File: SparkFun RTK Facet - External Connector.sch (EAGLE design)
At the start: 29 parts, among them J1 Qwiic, J3 ESP32 USB, J4 Qwiic, J5 u-blox USB

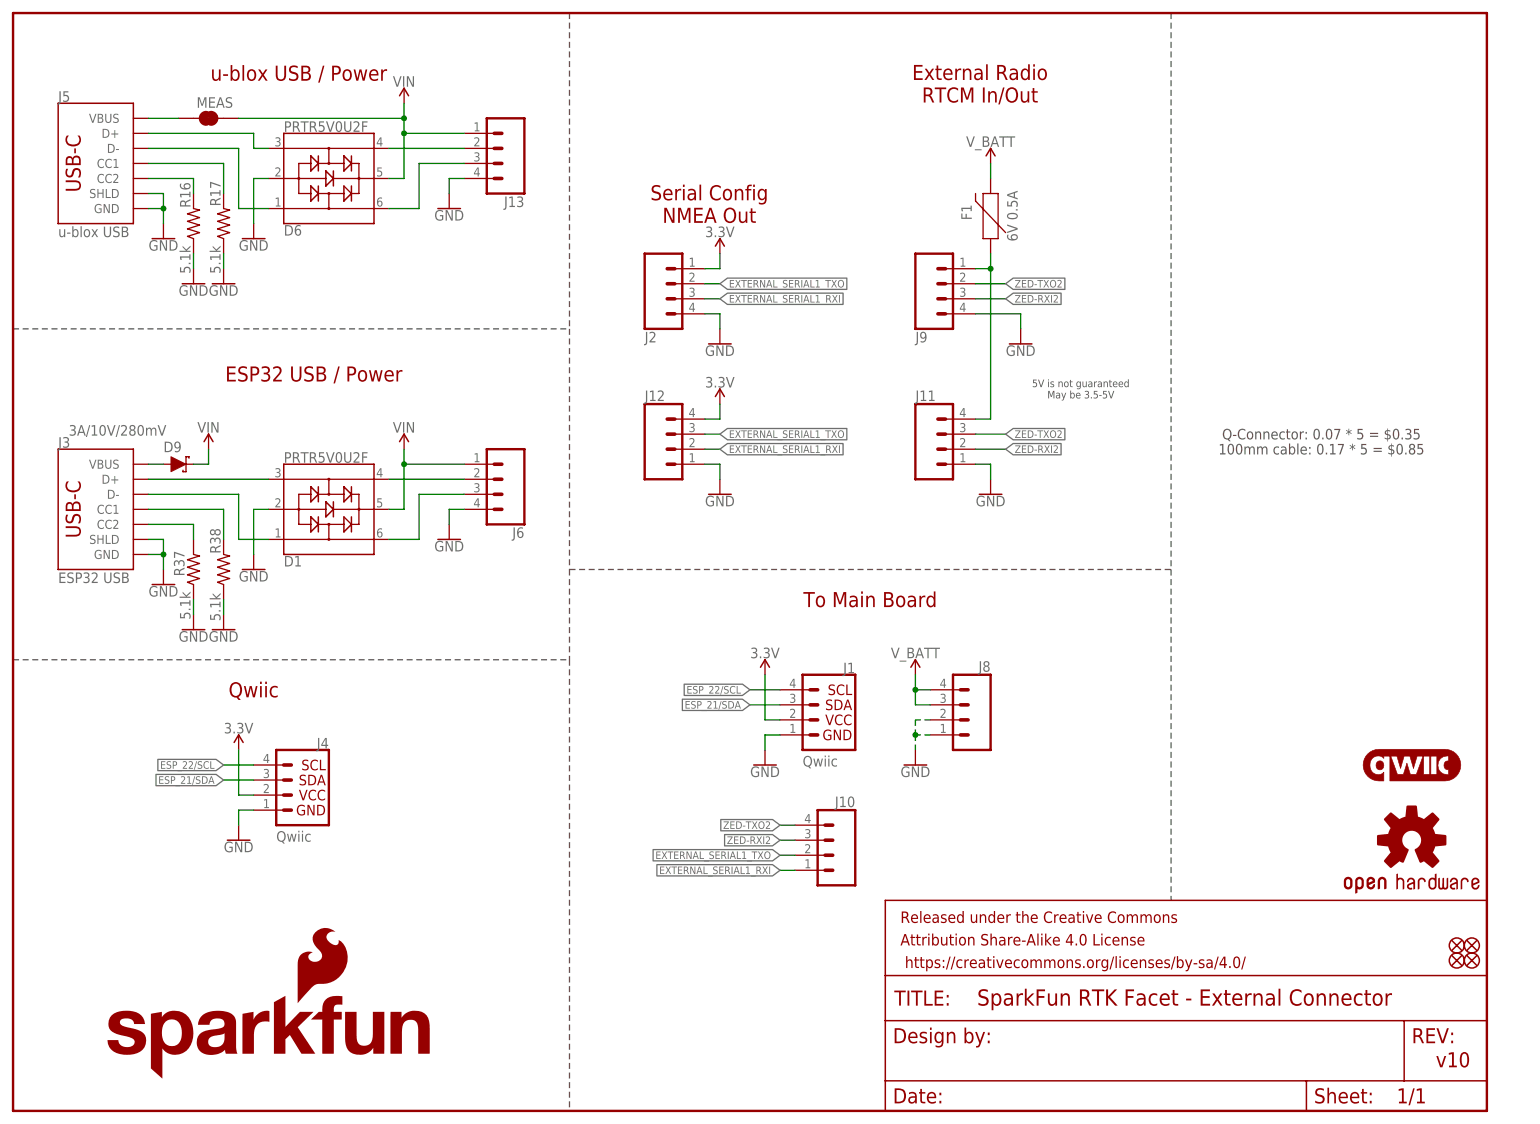
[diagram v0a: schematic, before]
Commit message: Add 22ohm to USB hub D+/D-.
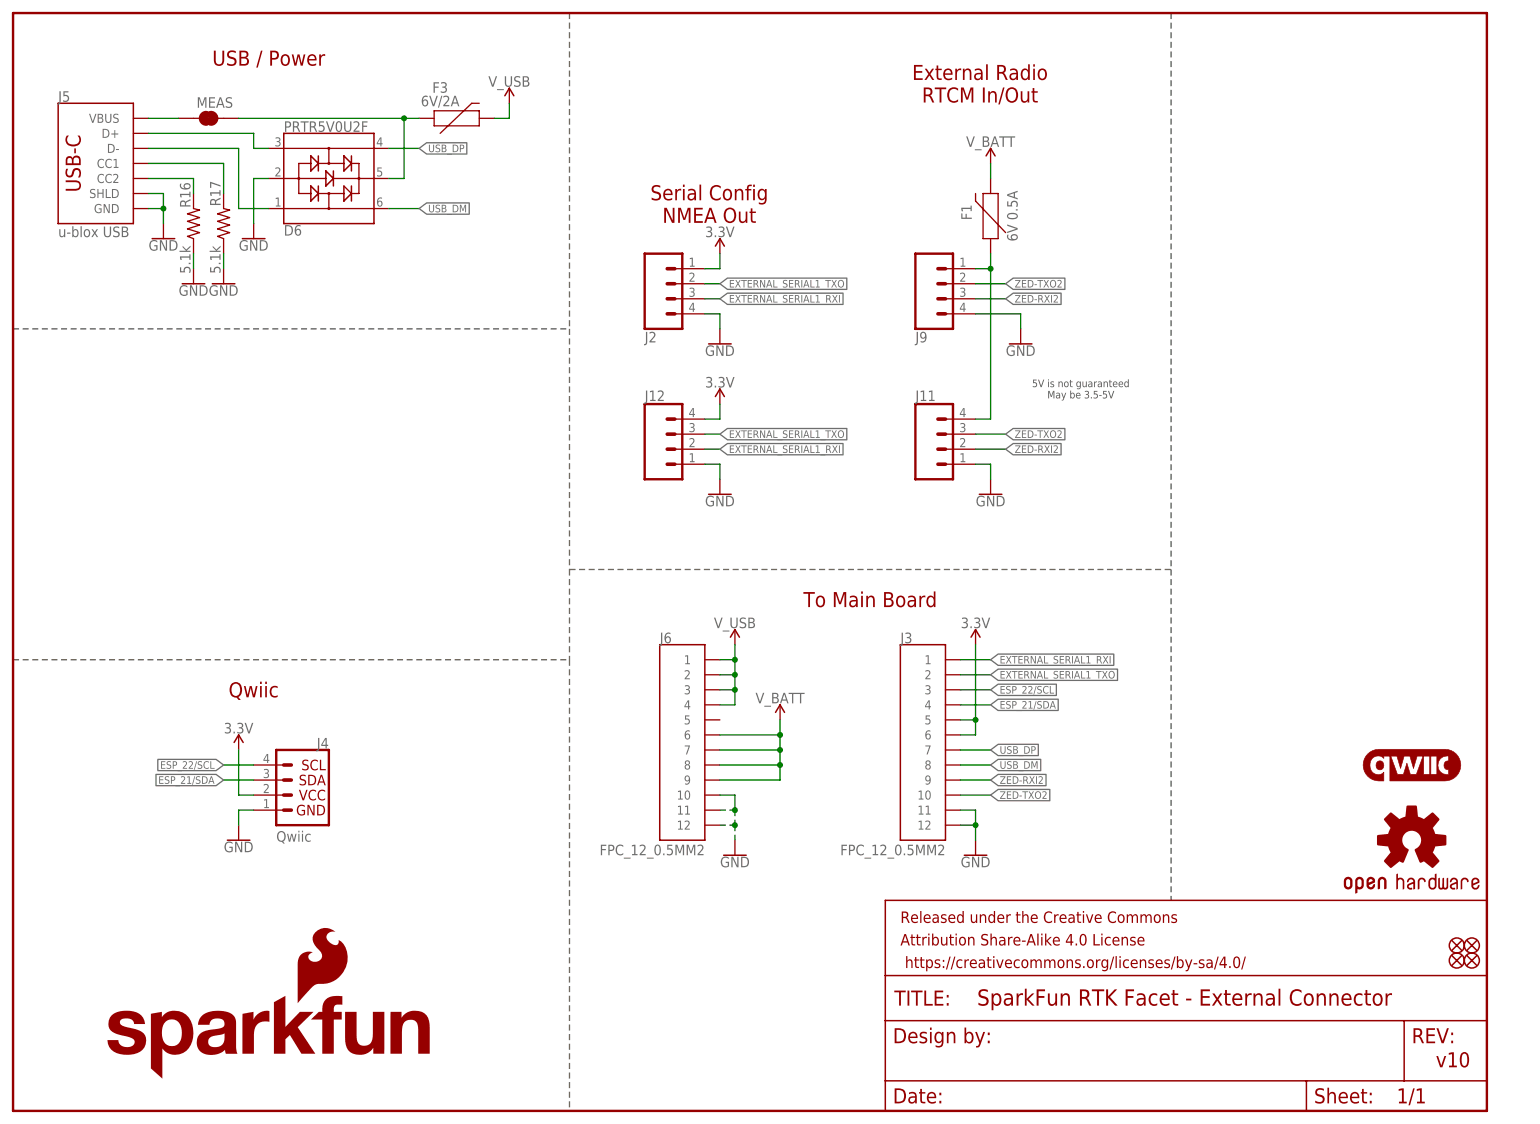
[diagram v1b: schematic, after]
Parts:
- removed D1: PRTR5V0U2F, SparkFun-IC-Power:PRTR5V0U2F
- removed D9: 3A/10V/280mV, SparkFun-DiscreteSemi:DIODE-SCHOTTKY-BAT60A
- removed J1: Qwiic, SparkFun-Connectors:I2C_STANDARDQWIIC
- removed J10, J13, J8: (no value), SparkFun-Connectors:CONN_04SMD2
- removed R37, R38: 5.1k, SparkFun-Resistors:5.1KOHM5.1KOHM-0603-1/10W-1%
- added F3: 6V/2A, SparkFun-Fuses:PPTC_6V2A
- J3: value ESP32 USB -> FPC_12_0.5MM2; device SparkFun-Connectors:USB_C_2-LAYER_PADS -> RTK Facet:FPC_12_0.5MM2
- J6: value (none) -> FPC_12_0.5MM2; device SparkFun-Connectors:CONN_04SMD2 -> RTK Facet:FPC_12_0.5MM2
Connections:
- net UBX1_D_N renamed USB1_D_M
- net UBX1_D_P renamed USB1_D_P
- removed net CC3: J3.CC2, R37.2
- removed net CC4: J3.CC1, R38.2
- removed net ESP1_D_N: D1.1, J3.D-
- removed net ESP1_D_P: D1.3, J3.D+
- removed net ESP_D_N: D1.6, J6.3
- removed net ESP_D_P: D1.4, J6.2
- removed net N$32: D9.A, J3.VBUS
- removed net UBX_D_N: D6.6, J13.3
- removed net UBX_D_P: D6.4, J13.2
- removed net VIN: D1.5, D6.5, D9.C, J13.1, J6.1, MEAS.2
- new net N$1: D6.5, F3.1, MEAS.2
- new net USB_DM: D6.6, J3.8
- new net USB_DP: D6.4, J3.7
- new net V_USB: F3.2, J6.1, J6.2, J6.3, J6.4
- net 3.3V: now also J3.5, J3.6; no longer J1.2
- net ESP_21/SDA: now also J3.4; no longer J1.3
- net ESP_22/SCL: now also J3.3; no longer J1.4
- net EXTERNAL_SERIAL1_RXI: now also J3.1; no longer J10.1
- net EXTERNAL_SERIAL1_TXO: now also J3.2; no longer J10.2
- net GND: now also J3.11, J3.12, J6.10, J6.11, J6.12; no longer D1.2, J1.1, J13.4, J3.GND, J3.SHLD, J6.4, J8.1, J8.2, R37.1, R38.1
- net V_BATT: now also J6.6, J6.7, J6.8, J6.9; no longer J8.3, J8.4
- net ZED-RXI2: now also J3.9; no longer J10.3
- net ZED-TXO2: now also J3.10; no longer J10.4
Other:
- note added: "USB / Power"
- note removed: "100mm cable: 0.17 * 5 = $0.85"
- note removed: "ESP32 USB / Power"
- note removed: "Q-Connector: 0.07 * 5 = $0.35"
- note removed: "u-blox USB / Power"

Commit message: Fix errors on all 3 boards after enclosure review.
* Flip connector board completely. Mirror connectors.
* Mirror connector on SD board
* Move LED above SIM socket
* Add membrane connector to SD board
* Remove switch connector from main board
* Increase width of connector board, 2mm on each side - 54mm wide
* Move LiPo Connector north as much as possible
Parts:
- removed J3: FPC_12_0.5MM2, RTK Facet:FPC_12_0.5MM2
- added J1: FPC_12_0.5MM2, RTK Facet:FPC_12_0.5MM2
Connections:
- net N$1 renamed VIN1
- net N$4 renamed VIN
- net 3.3V: now also J6.7, J6.8; no longer J3.5, J3.6
- net ESP_21/SDA: now also J6.9; no longer J3.4
- net ESP_22/SCL: now also J6.10; no longer J3.3
- net EXTERNAL_SERIAL1_RXI: now also J6.12; no longer J3.1
- net EXTERNAL_SERIAL1_TXO: now also J6.11; no longer J3.2
- net GND: now also J1.1, J1.2, J1.3, J6.1, J6.2; no longer J3.11, J3.12, J6.10, J6.11, J6.12
- net USB_DM: now also J6.5; no longer J3.8
- net USB_DP: now also J6.6; no longer J3.7
- net V_BATT: now also J1.4, J1.5, J1.6, J1.7; no longer J6.6, J6.7, J6.8, J6.9
- net V_USB: now also J1.10, J1.11, J1.12, J1.9; no longer J6.1, J6.2, J6.3, J6.4
- net ZED-RXI2: now also J6.4; no longer J3.9
- net ZED-TXO2: now also J6.3; no longer J3.10
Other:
- moved on the sheet: J6
